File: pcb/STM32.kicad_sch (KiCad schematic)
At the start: 4 parts, among them CN1 Conn_02x08_Odd_Even, CN2 Conn_02x15_Odd_Even, CN3 Conn_02x10_Odd_Even, CN4 Conn_02x17_Odd_Even

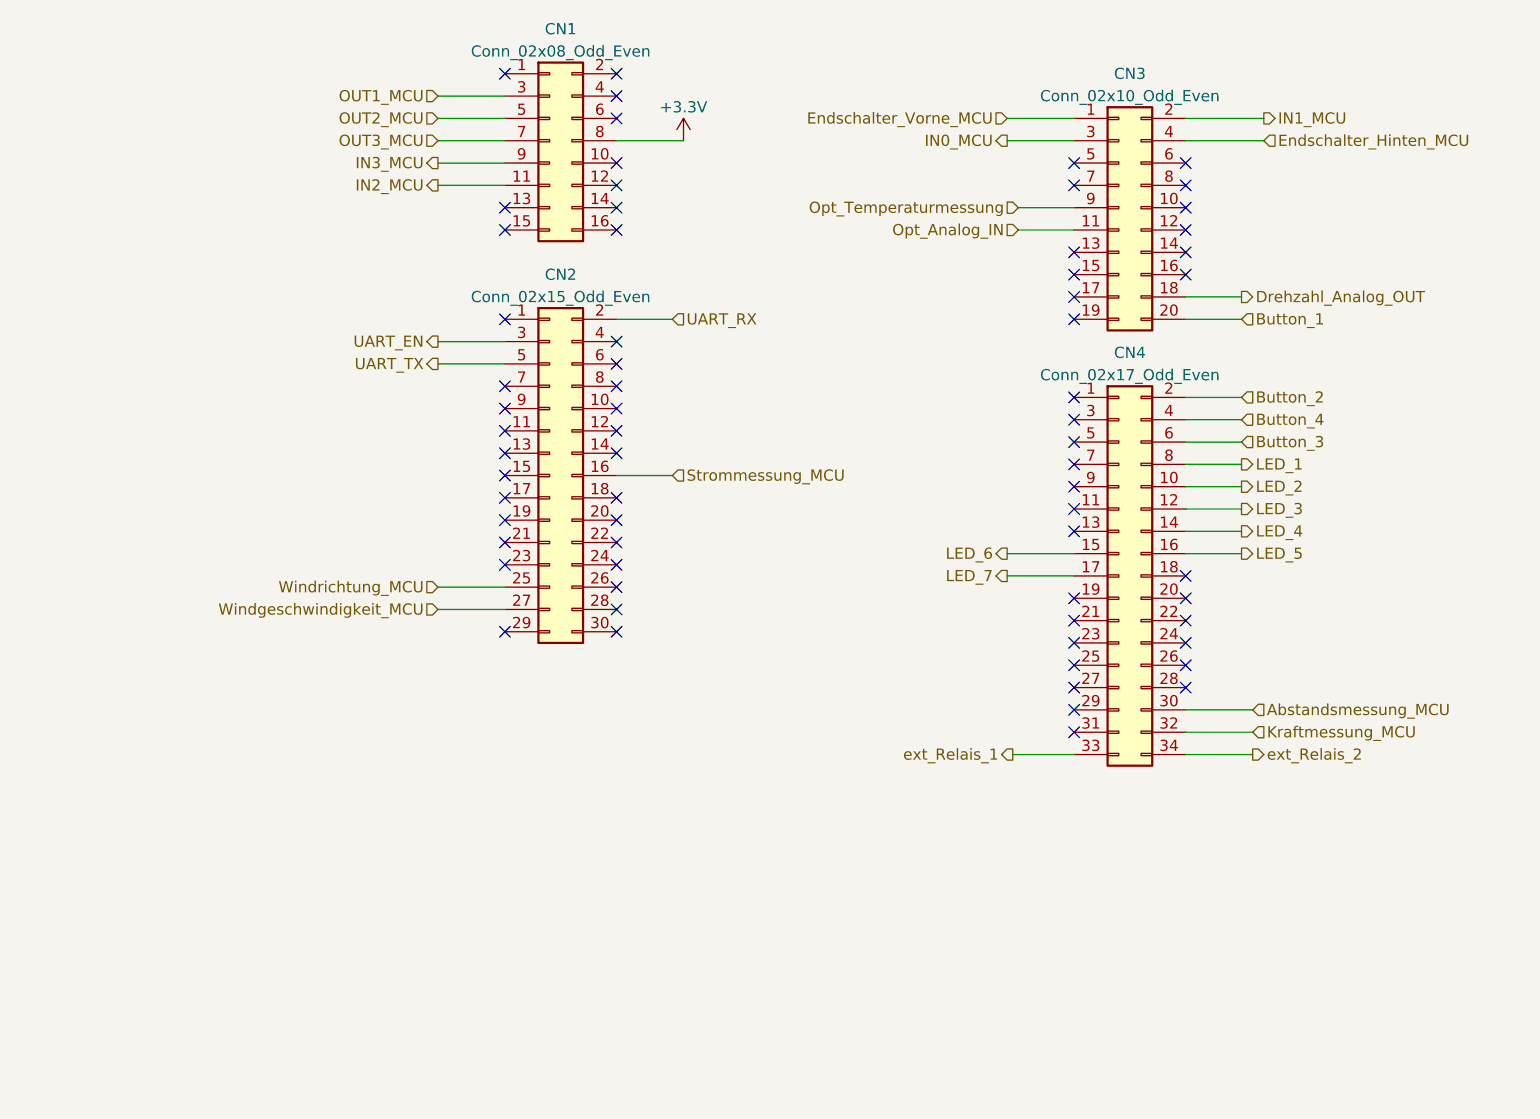
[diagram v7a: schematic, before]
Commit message: added voltage regulator updated pinout
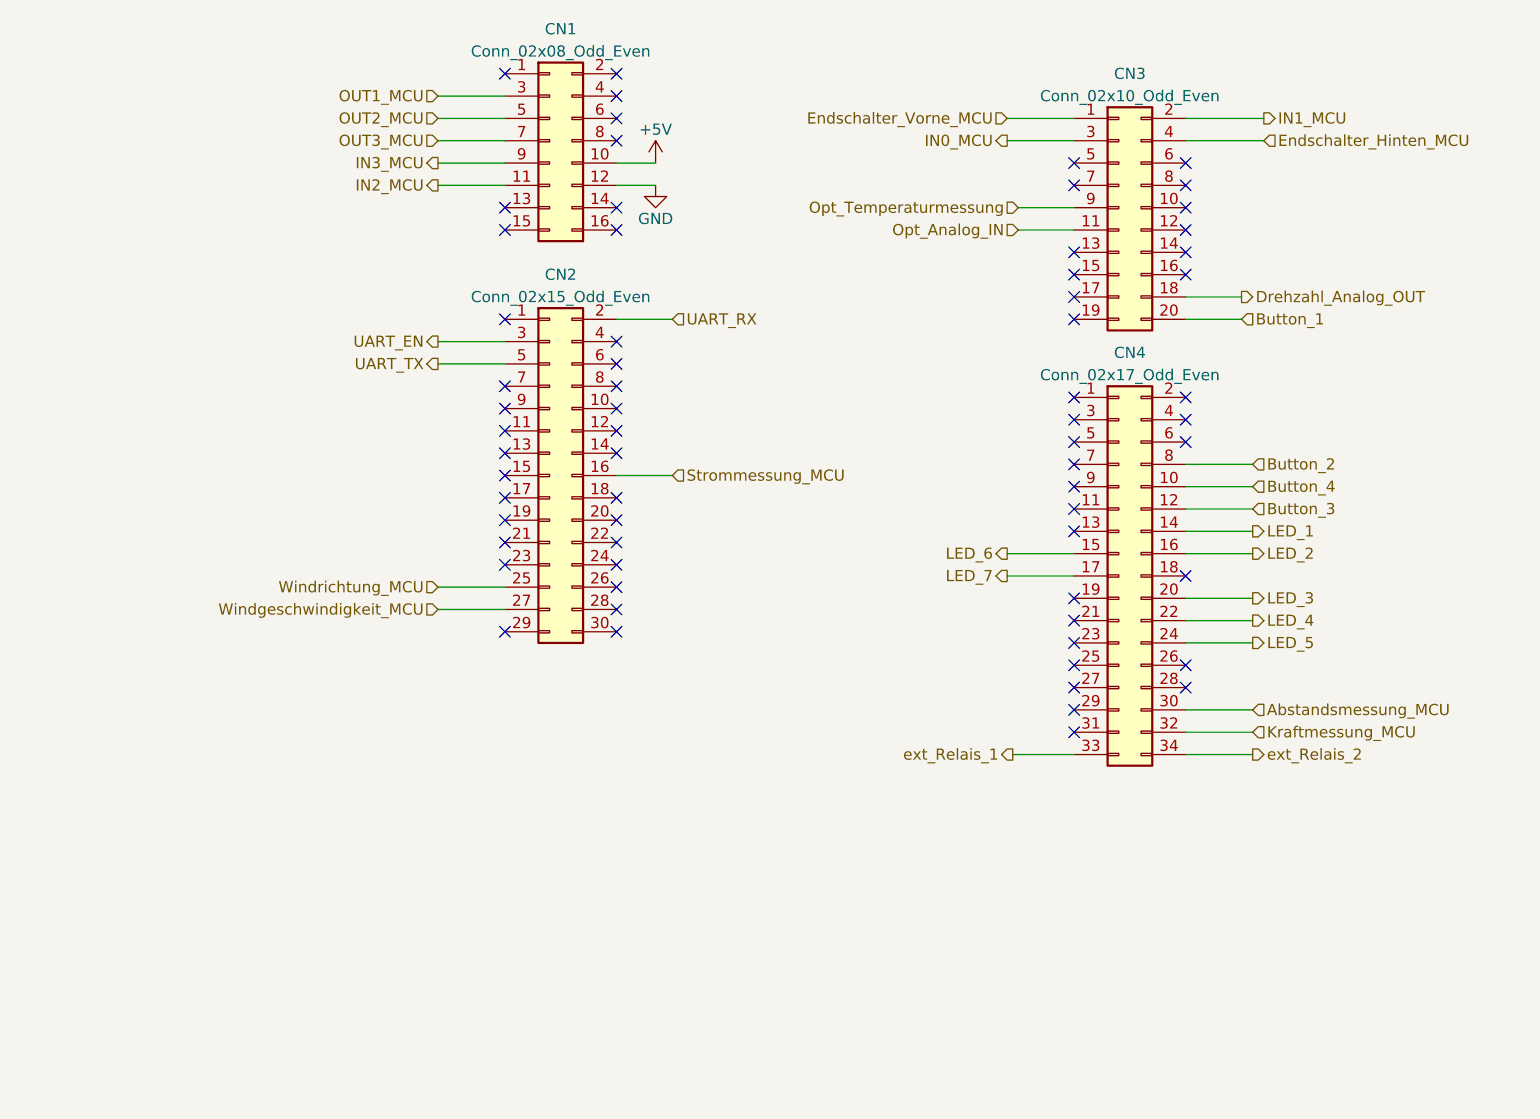
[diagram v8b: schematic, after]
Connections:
- net Button_2: now also CN4.8 (Pin_8); no longer CN4.2 (Pin_2)
- net Button_3: now also CN4.12 (Pin_12); no longer CN4.6 (Pin_6)
- net Button_4: now also CN4.10 (Pin_10); no longer CN4.4 (Pin_4)
- net LED_1: now also CN4.14 (Pin_14); no longer CN4.8 (Pin_8)
- net LED_2: now also CN4.16 (Pin_16); no longer CN4.10 (Pin_10)
- net LED_3: now also CN4.20 (Pin_20); no longer CN4.12 (Pin_12)
- net LED_4: now also CN4.22 (Pin_22); no longer CN4.14 (Pin_14)
- net LED_5: now also CN4.24 (Pin_24); no longer CN4.16 (Pin_16)
- net +5V: now reaches CN1.10 (Pin_10)
- net GND: now reaches CN1.12 (Pin_12)
- net +3.3V: no longer names the net of CN1.8 (Pin_8)
- no-connect marks 66 -> 65
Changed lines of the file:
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@@
   (no_connect (at 96.52 43.18))
   (no_connect (at 161.29 71.12))
-  (no_connect (at 173.99 105.41))
   (no_connect (at 161.29 53.34))
   (no_connect (at 96.52 88.9))
+  (no_connect (at 173.99 100.33))
   (no_connect (at 96.52 58.42))
-  (no_connect (at 173.99 107.95))
   (no_connect (at 109.22 45.72))
   (no_connect (at 161.29 68.58))
+  (no_connect (at 173.99 80.01))
   (no_connect (at 109.22 81.28))
   (no_connect (at 96.52 78.74))
   (no_connect (at 109.22 99.06))
   (no_connect (at 161.29 63.5))
-  (no_connect (at 173.99 100.33))
   (no_connect (at 173.99 66.04))
   (no_connect (at 161.29 80.01))
@@
   (no_connect (at 161.29 87.63))
   (no_connect (at 161.29 110.49))
-  (no_connect (at 109.22 55.88))
   (no_connect (at 173.99 55.88))
   (no_connect (at 109.22 93.98))
   (no_connect (at 109.22 76.2))
+  (no_connect (at 173.99 85.09))
   (no_connect (at 161.29 55.88))
   (no_connect (at 173.99 63.5))
+  (no_connect (at 173.99 82.55))
   (no_connect (at 109.22 43.18))
   (no_connect (at 96.52 86.36))
@@
   (no_connect (at 173.99 60.96))
   (no_connect (at 173.99 113.03))
-  (no_connect (at 109.22 53.34))
+  (no_connect (at 109.22 50.8))
   (no_connect (at 109.22 58.42))
   (no_connect (at 109.22 60.96))
@@
   (no_connect (at 96.52 81.28))
   (no_connect (at 161.29 113.03))
-  (no_connect (at 173.99 102.87))
   (no_connect (at 161.29 105.41))
   (no_connect (at 161.29 92.71))
   (no_connect (at 96.52 106.68))
   (no_connect (at 173.99 53.34))
+  (wire (pts (xy 173.99 102.87) (xy 181.61 102.87))
+    (stroke (width 0) (type default))
+  )
+  (wire (pts (xy 173.99 97.79) (xy 181.61 97.79))
+    (stroke (width 0) (type default))
+  )
+  (wire (pts (xy 173.99 95.25) (xy 181.61 95.25))
+    (stroke (width 0) (type default))
+  )
+  (wire (pts (xy 109.22 53.34) (xy 113.665 53.34))
+    (stroke (width 0) (type default))
+  )
   (wire (pts (xy 154.305 120.65) (xy 161.29 120.65))
     (stroke (width 0) (type default))
   )
+  (wire (pts (xy 109.22 55.88) (xy 113.665 55.88))
+    (stroke (width 0) (type default))
+  )
   (wire (pts (xy 88.9 53.34) (xy 96.52 53.34))
     (stroke (width 0) (type default))
   )
-  (wire (pts (xy 173.99 82.55) (xy 180.34 82.55))
+  (wire (pts (xy 173.99 90.17) (xy 181.61 90.17))
     (stroke (width 0) (type default))
   )
@@
     (stroke (width 0) (type default))
   )
-  (wire (pts (xy 173.99 92.71) (xy 180.34 92.71))
-    (stroke (width 0) (type default))
-  )
   (wire (pts (xy 115.57 71.12) (xy 109.22 71.12))
     (stroke (width 0) (type default))
   )
-  (wire (pts (xy 173.99 95.25) (xy 180.34 95.25))
-    (stroke (width 0) (type default))
-  )
-  (wire (pts (xy 173.99 97.79) (xy 180.34 97.79))
+  (wire (pts (xy 173.99 105.41) (xy 181.61 105.41))
     (stroke (width 0) (type default))
   )
@@
     (stroke (width 0) (type default))
   )
+  (wire (pts (xy 173.99 107.95) (xy 181.61 107.95))
+    (stroke (width 0) (type default))
+  )
   (wire (pts (xy 88.9 48.26) (xy 96.52 48.26))
     (stroke (width 0) (type default))
@@
     (stroke (width 0) (type default))
   )
-  (wire (pts (xy 173.99 90.17) (xy 180.34 90.17))
+  (wire (pts (xy 173.99 87.63) (xy 181.61 87.63))
     (stroke (width 0) (type default))
   )
@@
     (stroke (width 0) (type default))
   )
-  (wire (pts (xy 116.84 50.8) (xy 109.22 50.8))
-    (stroke (width 0) (type default))
-  )
   (wire (pts (xy 154.94 60.96) (xy 161.29 60.96))
     (stroke (width 0) (type default))
@@
     (stroke (width 0) (type default))
   )
-  (wire (pts (xy 173.99 85.09) (xy 180.34 85.09))
-    (stroke (width 0) (type default))
-  )
   (wire (pts (xy 173.99 120.65) (xy 181.61 120.65))
     (stroke (width 0) (type default))
@@
     (stroke (width 0) (type default))
   )
-  (wire (pts (xy 173.99 80.01) (xy 180.34 80.01))
-    (stroke (width 0) (type default))
-  )
   (wire (pts (xy 153.67 48.26) (xy 161.29 48.26))
     (stroke (width 0) (type default))
@@
     (stroke (width 0) (type default))
   )
-  (wire (pts (xy 173.99 87.63) (xy 180.34 87.63))
+  (wire (pts (xy 173.99 92.71) (xy 181.61 92.71))
     (stroke (width 0) (type default))
   )
@@
     (effects (font (size 1.27 1.27)) (justify left))
   )
-  (hierarchical_label "Button_2" (shape input) (at 180.34 80.01 0) (fields_autoplaced)
+  (hierarchical_label "Button_2" (shape input) (at 181.61 87.63 0) (fields_autoplaced)
     (effects (font (size 1.27 1.27)) (justify left))
   )
@@
     (effects (font (size 1.27 1.27)) (justify right))
   )
-  (hierarchical_label "LED_2" (shape output) (at 180.34 90.17 0) (fields_autoplaced)
+  (hierarchical_label "LED_2" (shape output) (at 181.61 97.79 0) (fields_autoplaced)
     (effects (font (size 1.27 1.27)) (justify left))
   )
@@
     (effects (font (size 1.27 1.27)) (justify right))
   )
-  (hierarchical_label "Button_4" (shape input) (at 180.34 82.55 0) (fields_autoplaced)
-    (effects (font (size 1.27 1.27)) (justify left))
-  )
-  (hierarchical_label "LED_4" (shape output) (at 180.34 95.25 0) (fields_autoplaced)
-    (effects (font (size 1.27 1.27)) (justify left))
-  )
-  (hierarchical_label "LED_5" (shape output) (at 180.34 97.79 0) (fields_autoplaced)
+  (hierarchical_label "Button_4" (shape input) (at 181.61 90.17 0) (fields_autoplaced)
+    (effects (font (size 1.27 1.27)) (justify left))
+  )
+  (hierarchical_label "LED_4" (shape output) (at 181.61 105.41 0) (fields_autoplaced)
+    (effects (font (size 1.27 1.27)) (justify left))
+  )
+  (hierarchical_label "LED_5" (shape output) (at 181.61 107.95 0) (fields_autoplaced)
     (effects (font (size 1.27 1.27)) (justify left))
   )
@@
     (effects (font (size 1.27 1.27)) (justify right))
   )
-  (hierarchical_label "LED_1" (shape output) (at 180.34 87.63 0) (fields_autoplaced)
+  (hierarchical_label "LED_1" (shape output) (at 181.61 95.25 0) (fields_autoplaced)
     (effects (font (size 1.27 1.27)) (justify left))
   )
@@
     (effects (font (size 1.27 1.27)) (justify right))
   )
-  (hierarchical_label "Button_3" (shape input) (at 180.34 85.09 0) (fields_autoplaced)
+  (hierarchical_label "Button_3" (shape input) (at 181.61 92.71 0) (fields_autoplaced)
     (effects (font (size 1.27 1.27)) (justify left))
   )
@@
     (effects (font (size 1.27 1.27)) (justify right))
   )
-  (hierarchical_label "LED_3" (shape output) (at 180.34 92.71 0) (fields_autoplaced)
+  (hierarchical_label "LED_3" (shape output) (at 181.61 102.87 0) (fields_autoplaced)
     (effects (font (size 1.27 1.27)) (justify left))
   )
@@
   (hierarchical_label "UART_TX" (shape output) (at 88.9 76.2 180) (fields_autoplaced)
     (effects (font (size 1.27 1.27)) (justify right))
+  )
+  (symbol (lib_id "power:+5V") (at 113.665 53.34 0) (unit 1)
+    (in_bom yes) (on_board yes) (dnp no) (fields_autoplaced)
+    (property "Reference" "#PWR011" (at 113.665 57.15 0)
+      (effects (font (size 1.27 1.27)) hide)
+    )
+    (property "Value" "+5V" (at 113.665 49.53 0)
+      (effects (font (size 1.27 1.27)))
+    )
+    (property "Footprint" "" (at 113.665 53.34 0)
+      (effects (font (size 1.27 1.27)) hide)
+    )
+    (property "Datasheet" "" (at 113.665 53.34 0)
+      (effects (font (size 1.27 1.27)) hide)
+    )
+    (pin "1")
+    (instances
+      (project "STM32_F439ZI_Shield"
+        (path "/19bff231-ff37-4a40-bd06-2039e9f55c77/9c6dbdee-9d8a-4cc8-8ceb-3d83c2e63e3b"
+          (reference "#PWR011") (unit 1)
+        )
+      )
+    )
+  )
+  (symbol (lib_id "power:GND") (at 113.665 55.88 0) (unit 1)
+    (in_bom yes) (on_board yes) (dnp no)
+    (property "Reference" "#PWR092" (at 113.665 62.23 0)
+      (effects (font (size 1.27 1.27)) hide)
+    )
+    (property "Value" "GND" (at 113.665 59.69 0)
+      (effects (font (size 1.27 1.27)))
+    )
+    (property "Footprint" "" (at 113.665 55.88 0)
+      (effects (font (size 1.27 1.27)) hide)
+    )
+    (property "Datasheet" "" (at 113.665 55.88 0)
+      (effects (font (size 1.27 1.27)) hide)
+    )
+    (pin "1")
+    (instances
+      (project "STM32_F439ZI_Shield"
+        (path "/19bff231-ff37-4a40-bd06-2039e9f55c77/9c6dbdee-9d8a-4cc8-8ceb-3d83c2e63e3b"
+          (reference "#PWR092") (unit 1)
+        )
+      )
+    )
   )
   (symbol (lib_id "Connector_Generic:Conn_02x17_Odd_Even") (at 166.37 100.33 0) (unit 1)
@@
         )
       )
-    )
-  )
-  (symbol (lib_id "power:+3.3V") (at 116.84 50.8 0) (mirror y) (unit 1)
-    (in_bom yes) (on_board yes) (dnp no) (fields_autoplaced)
-    (property "Reference" "#PWR011" (at 116.84 54.61 0)
-      (effects (font (size 1.27 1.27)) hide)
-    )
-    (property "Value" "+3.3V" (at 116.84 46.99 0)
-      (effects (font (size 1.27 1.27)))
-    )
-    (property "Footprint" "" (at 116.84 50.8 0)
-      (effects (font (size 1.27 1.27)) hide)
-    )
-    (property "Datasheet" "" (at 116.84 50.8 0)
-      (effects (font (size 1.27 1.27)) hide)
-    )
-    (pin "1")
-    (instances
-      (project "STM32_F439ZI_Shield"
-        (path "/19bff231-ff37-4a40-bd06-2039e9f55c77/9c6dbdee-9d8a-4cc8-8ceb-3d83c2e63e3b"
-          (reference "#PWR011") (unit 1)
-        )
-      )
